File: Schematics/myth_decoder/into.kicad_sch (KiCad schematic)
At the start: 5 parts, among them U1016 74AHC138, U1017 74HC238, U1018 74AHC138

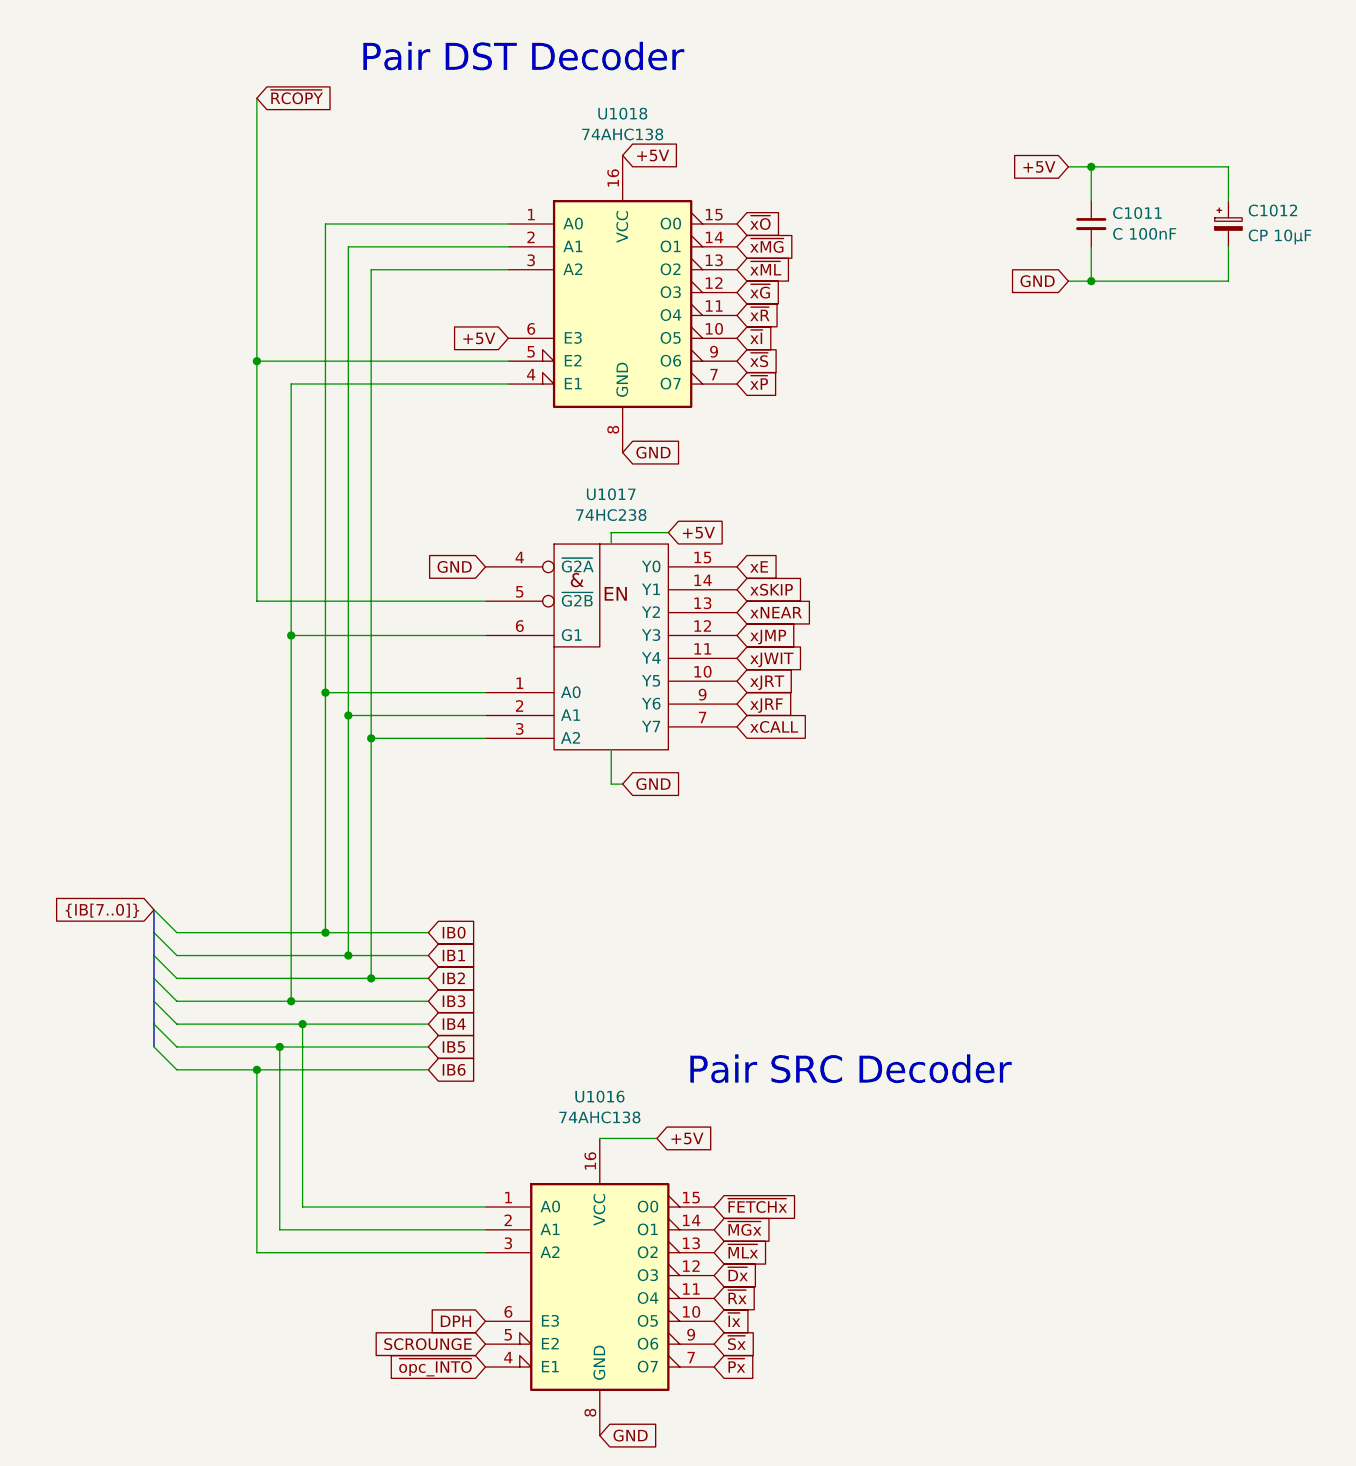
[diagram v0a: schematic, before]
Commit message: Let defines/labels diverge from assembler mnemonics
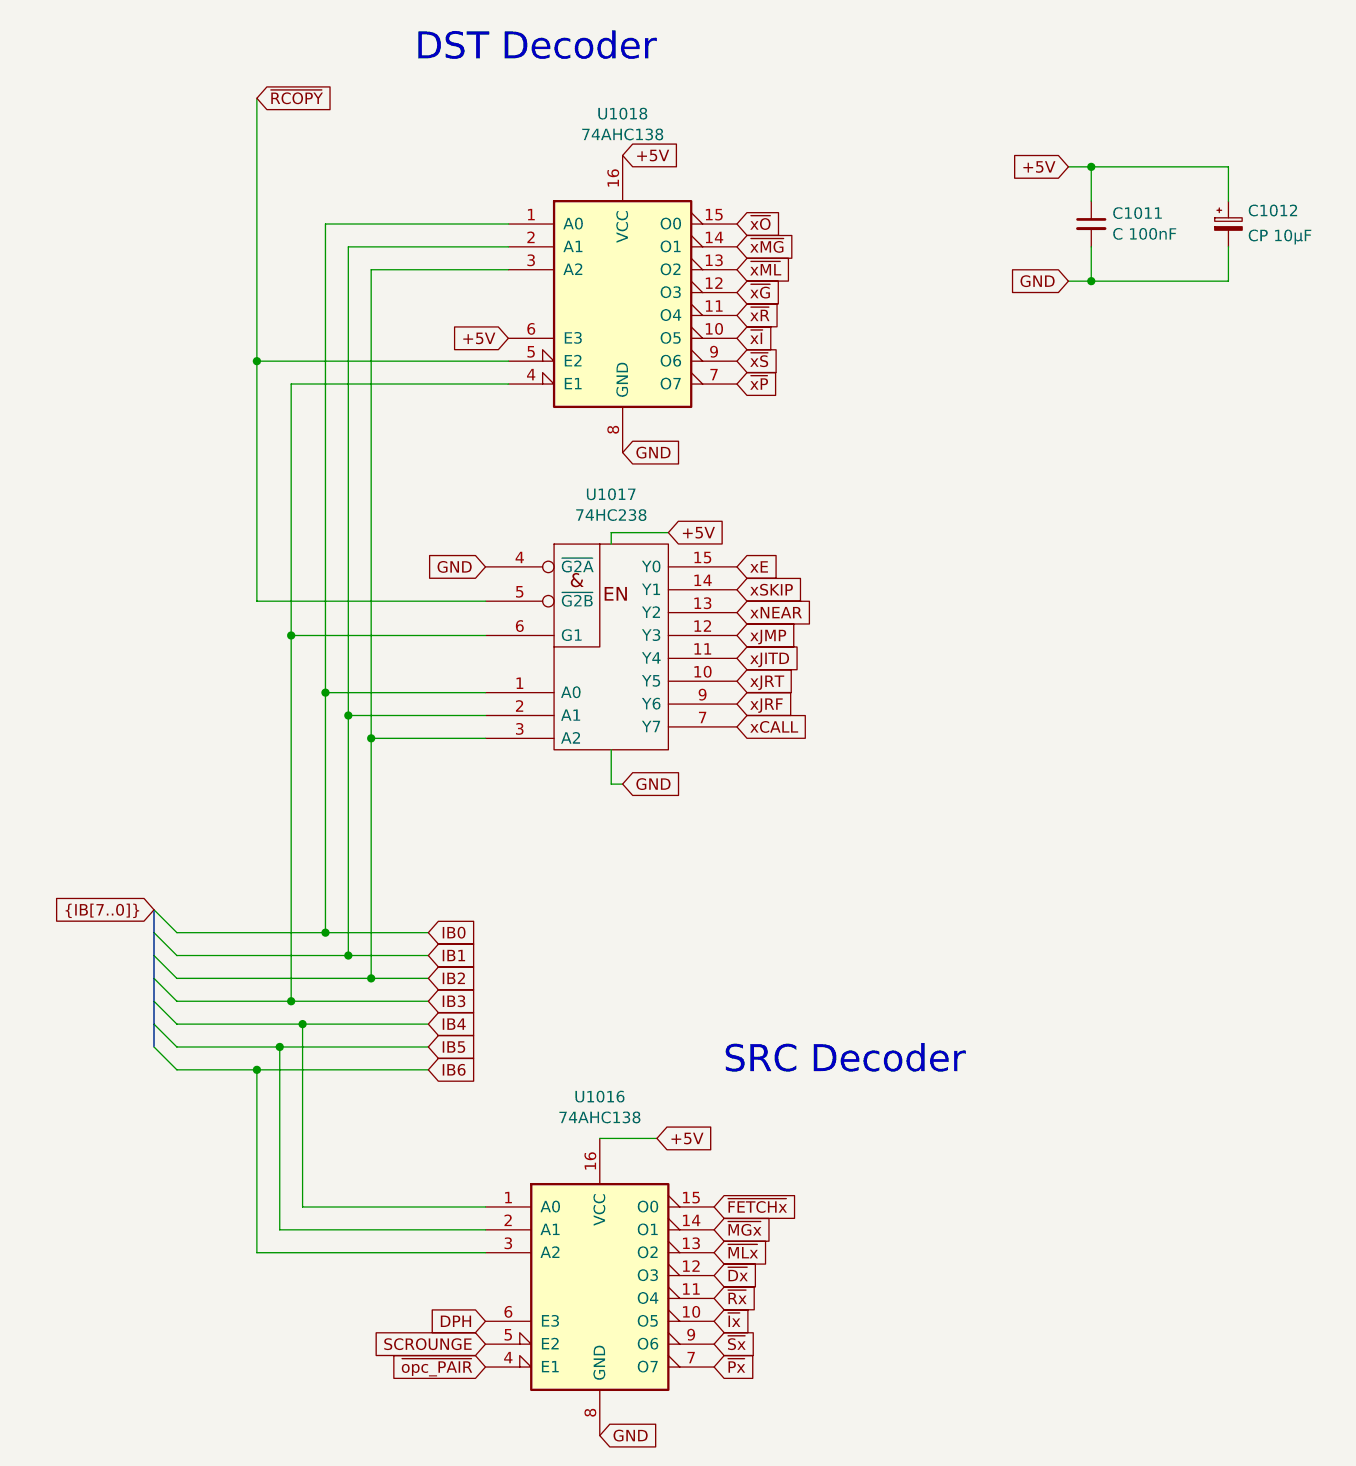
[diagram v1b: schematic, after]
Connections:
- net xJWIT renamed xJITD
- net ~{opc_INTO} renamed ~{opc_PAIR}
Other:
- note added: "DST Decoder"
- note added: "SRC Decoder"
- note removed: "Pair DST Decoder"
- note removed: "Pair SRC Decoder"
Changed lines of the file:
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@@
 		)
 	)
-	(text "Pair SRC Decoder"
+	(text "SRC Decoder"
 		(exclude_from_sim no)
-		(at 129.032 140.462 0)
+		(at 133.096 139.192 0)
 		(effects
 			(font
@@
 		)
 	)
-	(text "Pair DST Decoder"
+	(text "DST Decoder"
 		(exclude_from_sim no)
-		(at 92.71 27.94 0)
+		(at 98.806 26.67 0)
 		(effects
 			(font
@@
 		)
 	)
-	(global_label "~{opc_INTO}"
+	(global_label "~{opc_PAIR}"
 		(shape input)
 		(at 106.68 171.45 180)
@@
 		)
 	)
-	(global_label "xJWIT"
+	(global_label "xJITD"
 		(shape input)
 		(at 134.62 92.71 0)
